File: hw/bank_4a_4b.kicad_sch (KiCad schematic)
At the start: 4 parts, among them U1002 T20Q144xx

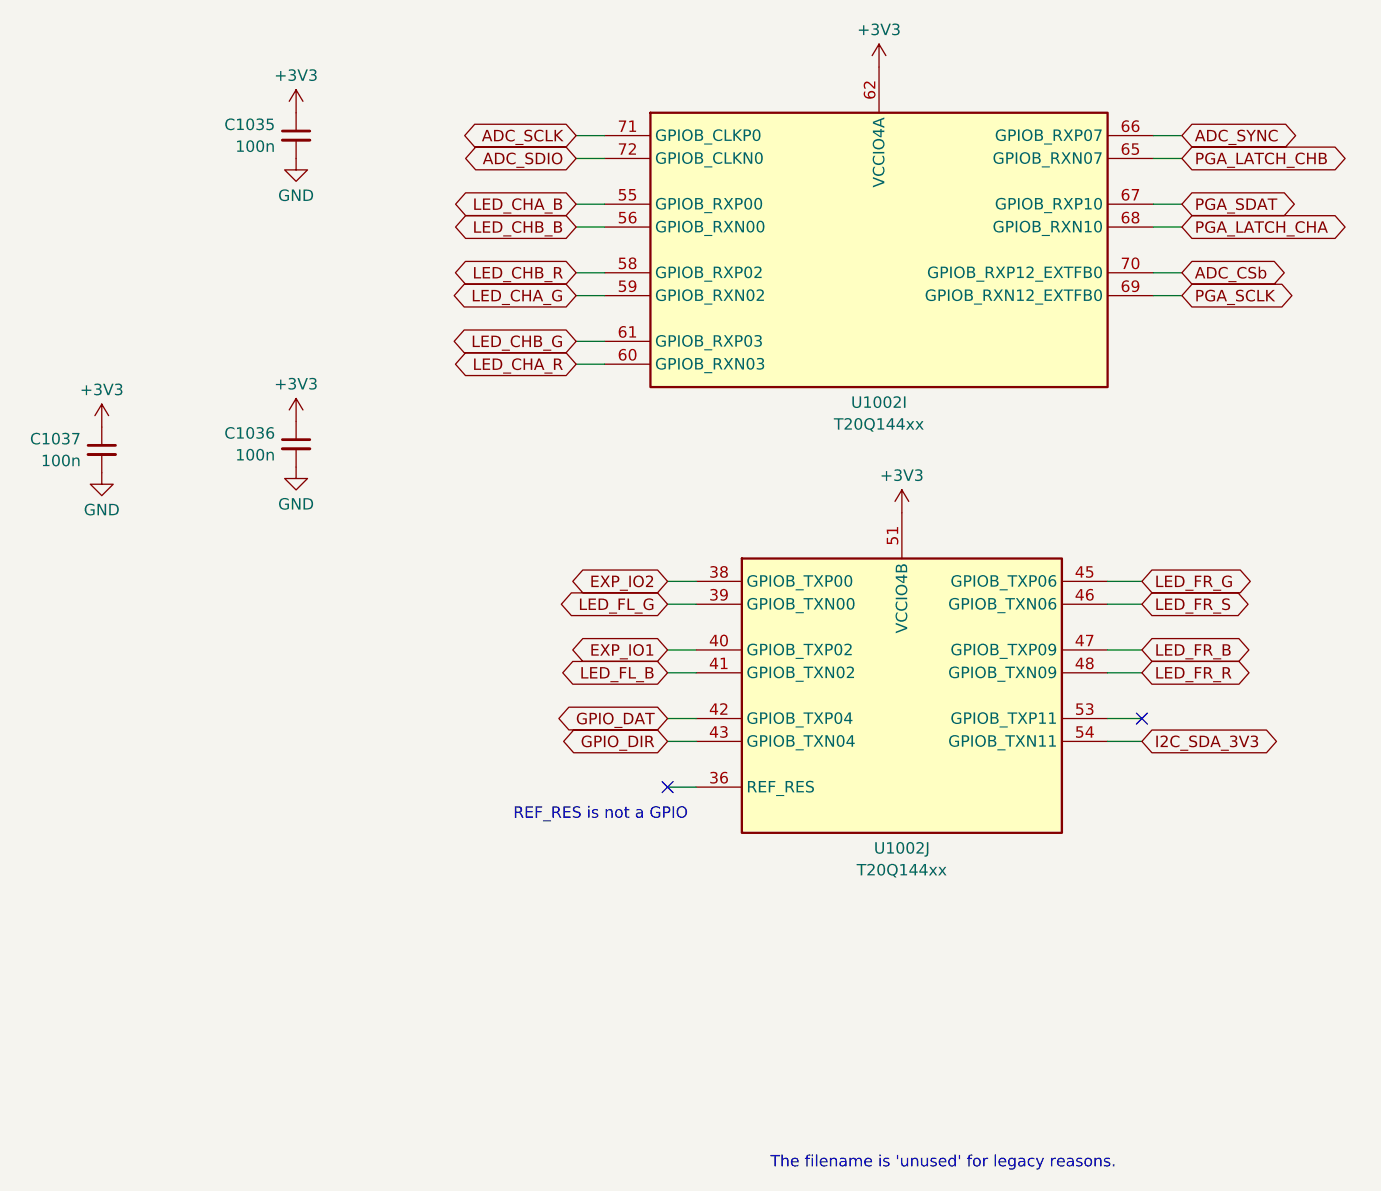
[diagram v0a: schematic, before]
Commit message: renumbered references on trion sub-sheets
Had used numbers > 1000 when merging designs
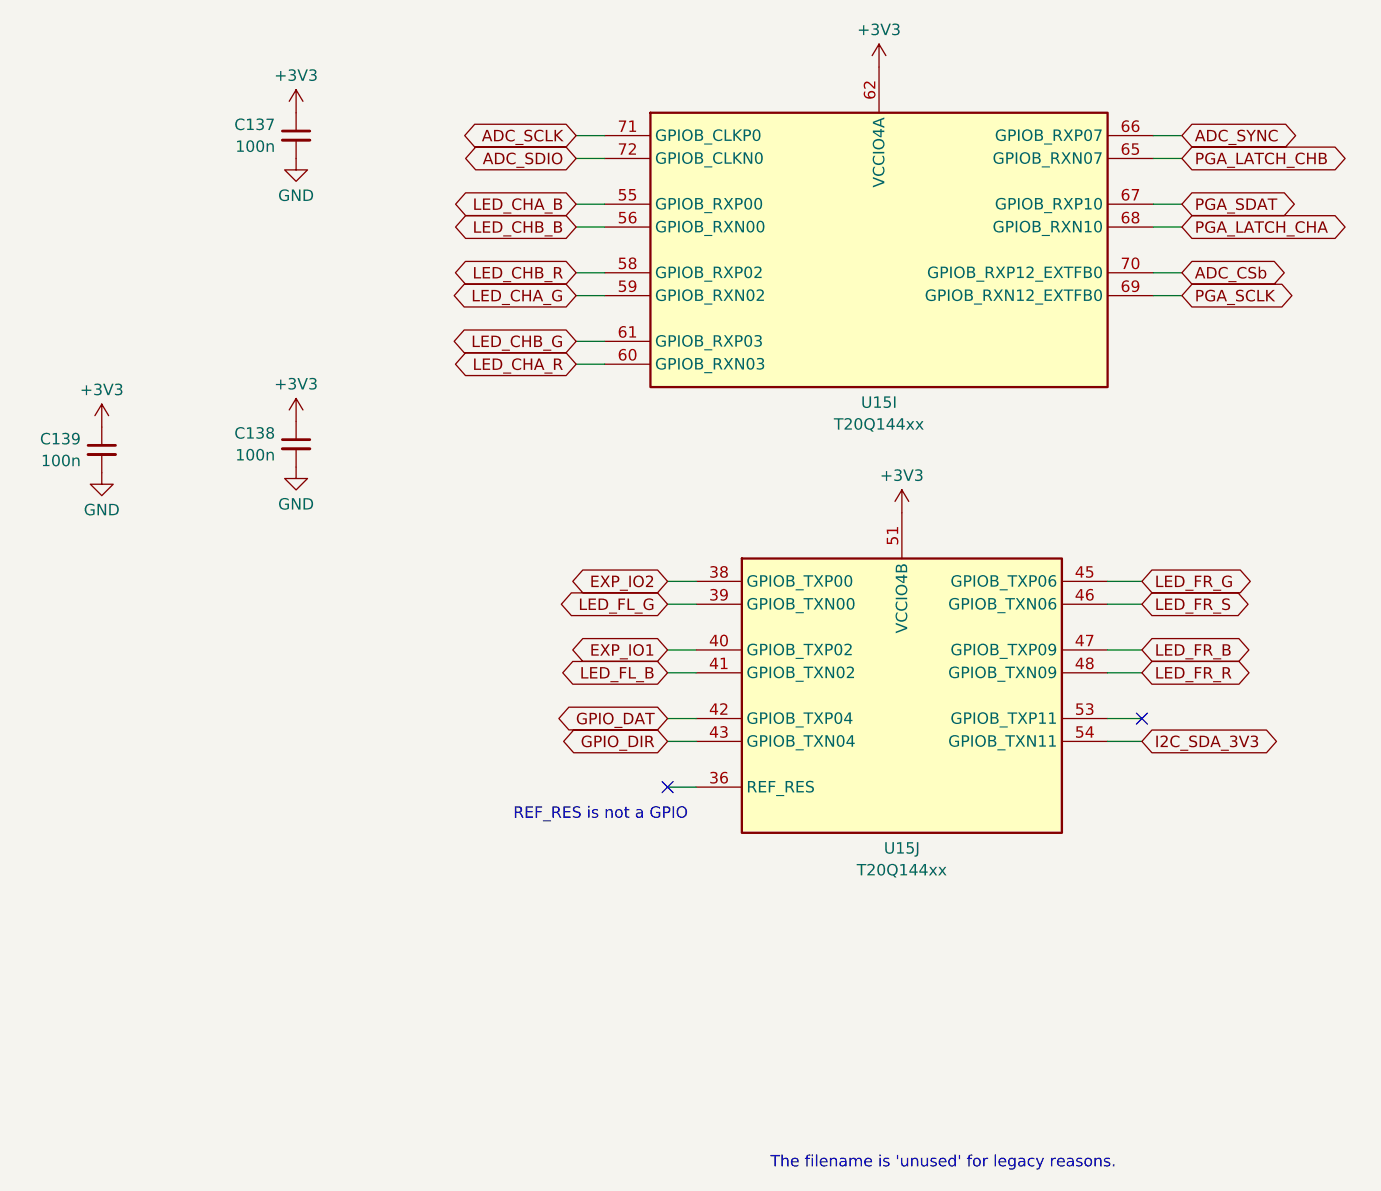
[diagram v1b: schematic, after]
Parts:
- renumbered C1035 to C137, C1036 to C138, C1037 to C139, U1002 to U15
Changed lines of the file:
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@@
   (symbol (lib_id "Device:C_Small") (at 127 63.5 0) (mirror y) (unit 1)
     (in_bom yes) (on_board yes) (dnp no) (fields_autoplaced)
-    (property "Reference" "C1035" (at 124.6759 62.2942 0)
+    (property "Reference" "C137" (at 124.6759 62.2942 0)
       (effects (font (size 1.27 1.27)) (justify left))
     )
@@
       (project "usbadc"
         (path "/7c8a1f8d-8834-4c9b-aaae-1f231e9b09a1/d9cd2a48-41b0-4b01-a978-0843576735ad/b37c57e6-fd28-4b13-a567-f707971d2f60"
+          (reference "C137") (unit 1)
+        )
+      )
+      (project "trion-8-test"
+        (path "/8c6e15e3-1804-4f03-8a4f-3cb8420d9169/b37c57e6-fd28-4b13-a567-f707971d2f60"
           (reference "C1035") (unit 1)
         )
       )
-      (project "trion-8-test"
-        (path "/8c6e15e3-1804-4f03-8a4f-3cb8420d9169/b37c57e6-fd28-4b13-a567-f707971d2f60"
-          (reference "C1035") (unit 1)
-        )
-      )
     )
   )
@@
   (symbol (lib_id "FPGA_Efinix_Trion:T8Q144xx") (at 194.31 125.73 0) (unit 10)
     (in_bom yes) (on_board yes) (dnp no) (fields_autoplaced)
-    (property "Reference" "U1002" (at 194.31 142.6901 0)
+    (property "Reference" "U15" (at 194.31 142.6901 0)
       (effects (font (size 1.27 1.27)))
     )
@@
       (project "usbadc"
         (path "/7c8a1f8d-8834-4c9b-aaae-1f231e9b09a1/d9cd2a48-41b0-4b01-a978-0843576735ad/b37c57e6-fd28-4b13-a567-f707971d2f60"
+          (reference "U15") (unit 10)
+        )
+      )
+      (project "trion-8-test"
+        (path "/8c6e15e3-1804-4f03-8a4f-3cb8420d9169/b37c57e6-fd28-4b13-a567-f707971d2f60"
           (reference "U1002") (unit 10)
         )
       )
-      (project "trion-8-test"
-        (path "/8c6e15e3-1804-4f03-8a4f-3cb8420d9169/b37c57e6-fd28-4b13-a567-f707971d2f60"
-          (reference "U1002") (unit 10)
-        )
-      )
     )
   )
@@
   (symbol (lib_id "FPGA_Efinix_Trion:T8Q144xx") (at 191.77 76.2 0) (unit 9)
     (in_bom yes) (on_board yes) (dnp no) (fields_autoplaced)
-    (property "Reference" "U1002" (at 191.77 93.1601 0)
+    (property "Reference" "U15" (at 191.77 93.1601 0)
       (effects (font (size 1.27 1.27)))
     )
@@
       (project "usbadc"
         (path "/7c8a1f8d-8834-4c9b-aaae-1f231e9b09a1/d9cd2a48-41b0-4b01-a978-0843576735ad/b37c57e6-fd28-4b13-a567-f707971d2f60"
+          (reference "U15") (unit 9)
+        )
+      )
+      (project "trion-8-test"
+        (path "/8c6e15e3-1804-4f03-8a4f-3cb8420d9169/b37c57e6-fd28-4b13-a567-f707971d2f60"
           (reference "U1002") (unit 9)
         )
       )
-      (project "trion-8-test"
-        (path "/8c6e15e3-1804-4f03-8a4f-3cb8420d9169/b37c57e6-fd28-4b13-a567-f707971d2f60"
-          (reference "U1002") (unit 9)
-        )
-      )
     )
   )
   (symbol (lib_id "Device:C_Small") (at 127 97.79 0) (mirror y) (unit 1)
     (in_bom yes) (on_board yes) (dnp no) (fields_autoplaced)
-    (property "Reference" "C1036" (at 124.6759 96.5842 0)
+    (property "Reference" "C138" (at 124.6759 96.5842 0)
       (effects (font (size 1.27 1.27)) (justify left))
     )
@@
       (project "usbadc"
         (path "/7c8a1f8d-8834-4c9b-aaae-1f231e9b09a1/d9cd2a48-41b0-4b01-a978-0843576735ad/b37c57e6-fd28-4b13-a567-f707971d2f60"
+          (reference "C138") (unit 1)
+        )
+      )
+      (project "trion-8-test"
+        (path "/8c6e15e3-1804-4f03-8a4f-3cb8420d9169/b37c57e6-fd28-4b13-a567-f707971d2f60"
           (reference "C1036") (unit 1)
         )
       )
-      (project "trion-8-test"
-        (path "/8c6e15e3-1804-4f03-8a4f-3cb8420d9169/b37c57e6-fd28-4b13-a567-f707971d2f60"
-          (reference "C1036") (unit 1)
-        )
-      )
     )
   )
   (symbol (lib_id "Device:C_Small") (at 105.41 98.425 0) (mirror y) (unit 1)
     (in_bom yes) (on_board yes) (dnp no) (fields_autoplaced)
-    (property "Reference" "C1037" (at 103.0859 97.2192 0)
+    (property "Reference" "C139" (at 103.0859 97.2192 0)
       (effects (font (size 1.27 1.27)) (justify left))
     )
@@
       (project "usbadc"
         (path "/7c8a1f8d-8834-4c9b-aaae-1f231e9b09a1/d9cd2a48-41b0-4b01-a978-0843576735ad/b37c57e6-fd28-4b13-a567-f707971d2f60"
-          (reference "C1037") (unit 1)
-        )
-      )
+          (reference "C139") (unit 1)
+        )
+      )

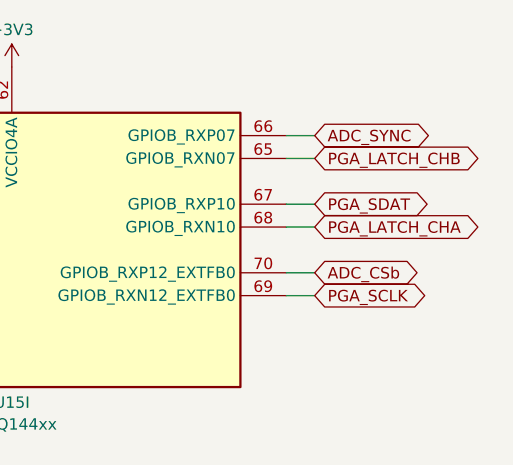
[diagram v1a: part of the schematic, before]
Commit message: PGA_SDAT / PGA_LATCH_CHB were swapped in top-sheet
 -> corrected there and swapped at FPGA bank keeps the
 layout unmodified but fixes the labels.
 => still compatible with v3.0 as ordered from JLC
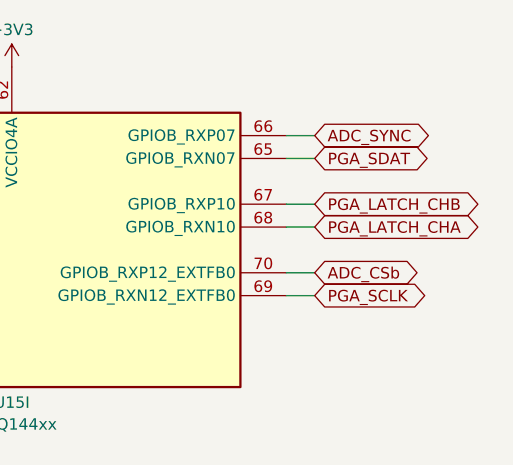
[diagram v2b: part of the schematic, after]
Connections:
- net PGA_LATCH_CHB: now also U15.67 (GPIOB_RXP10); no longer U15.65 (GPIOB_RXN07)
- net PGA_SDAT: now also U15.65 (GPIOB_RXN07); no longer U15.67 (GPIOB_RXP10)
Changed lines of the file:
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@@
     )
   )
-  (global_label "PGA_SDAT" (shape bidirectional) (at 225.425 71.12 0) (fields_autoplaced)
+  (global_label "PGA_SDAT" (shape bidirectional) (at 225.425 66.04 0) (fields_autoplaced)
     (effects (font (size 1.27 1.27)) (justify left))
-    (property "Intersheetrefs" "${INTERSHEET_REFS}" (at 237.8404 71.12 0)
+    (property "Intersheetrefs" "${INTERSHEET_REFS}" (at 237.8404 66.04 0)
       (effects (font (size 1.27 1.27)) (justify left) hide)
     )
@@
     )
   )
-  (global_label "PGA_LATCH_CHB" (shape bidirectional) (at 225.425 66.04 0) (fields_autoplaced)
+  (global_label "PGA_LATCH_CHB" (shape bidirectional) (at 225.425 71.12 0) (fields_autoplaced)
     (effects (font (size 1.27 1.27)) (justify left))
-    (property "Intersheetrefs" "${INTERSHEET_REFS}" (at 243.8276 66.04 0)
+    (property "Intersheetrefs" "${INTERSHEET_REFS}" (at 243.8276 71.12 0)
       (effects (font (size 1.27 1.27)) (justify left) hide)
     )

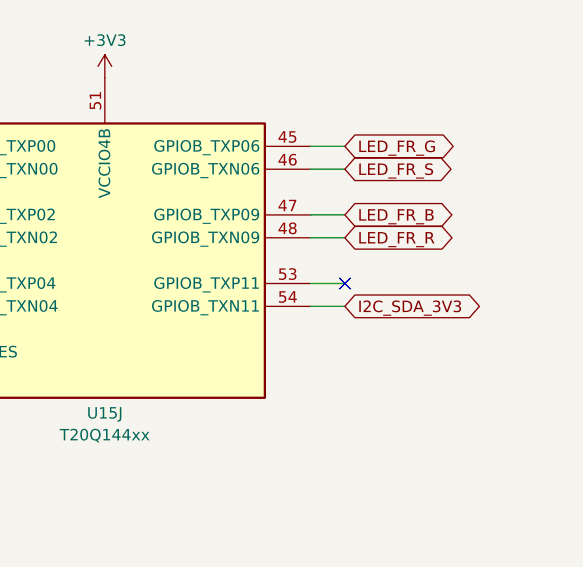
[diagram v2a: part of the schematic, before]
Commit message: Modified DAC resistors/range; connect + pull-up ADC SHDN
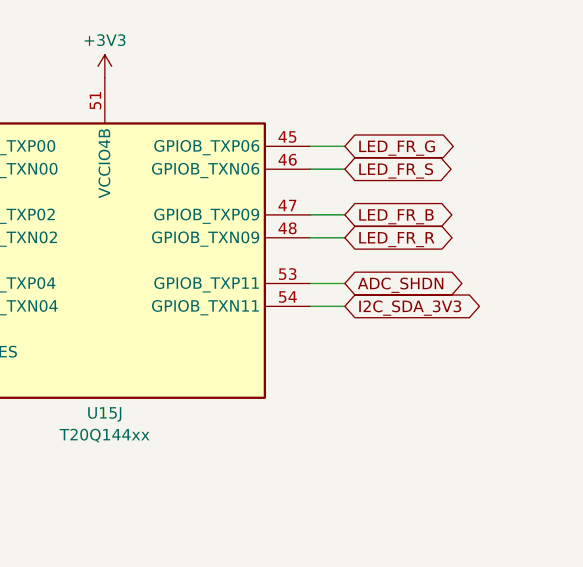
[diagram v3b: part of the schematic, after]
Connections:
- net ADC_SHDN: now reaches U15.53 (GPIOB_TXP11)
- no-connect marks 2 -> 1
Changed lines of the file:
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@@
   (paper "A4")
   (no_connect (at 168.275 135.89))
-  (no_connect (at 220.98 128.27))
   (wire (pts (xy 217.17 120.65) (xy 220.98 120.65))
     (stroke (width 0) (type default))
@@
     )
   )
+  (global_label "ADC_SHDN" (shape bidirectional) (at 220.98 128.27 0) (fields_autoplaced)
+    (effects (font (size 1.27 1.27)) (justify left))
+    (property "Intersheetrefs" "${INTERSHEET_REFS}" (at 234.0002 128.27 0)
+      (effects (font (size 1.27 1.27)) (justify left) hide)
+    )
+  )

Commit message: connected versaclock CLKSEL to ULPI RSTB (share FPGA pin)
ULPI Rstb is unlikely to be used

Also: - update of kicad to 9.0 (many library footprints updated)
      - added sheet titles, author
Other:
- company: (none) -> Till Straumann
- title: (none) -> FPGA Bank 4

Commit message: Added licensing information
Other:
- company: Till Straumann -> Copyright Till Straumann, 2025
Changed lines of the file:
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@@
 		(title "FPGA Bank 4")
 		(rev "3.3b")
-		(company "Till Straumann")
+		(company "Copyright Till Straumann, 2025")
+		(comment 1 "License: CERN-OHL-P v2")
 	)
 	(text "The filename is 'unused' for legacy reasons."
